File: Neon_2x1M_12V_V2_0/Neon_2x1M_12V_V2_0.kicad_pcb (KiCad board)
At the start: 2 copper layers, 60 x 59.5 mm, 32 parts, among them J2 Barrel_Jack_MountingPin, J6 Conn_01x03_Pin, J7 Screw_Terminal_01x02, J8 Screw_Terminal_01x02, Q1 IRLML2502TRPBF, Q2 IRLML2502TRPBF, SW1 SW_Push, SW2 SW_Push, U1 ESP32-WROOM-32, U3 LM2596T-ADJ

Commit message: updated production files
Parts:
- moved R7 2.67 mm to (166.0, 102.0)
- moved SW1 2.28 mm to (165.4, 107.5)
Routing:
- net ESP_EN: track 6.59 -> 11.3 mm
- net +3V3: track 75.4 -> 77.7 mm
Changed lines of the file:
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@@
 		(tags "connector JST NV vertical")
 		(property "Reference" "J8"
-			(at 9 4.55 0)
+			(at 8.7 4.15 0)
 			(layer "F.SilkS")
 			(effects
@@
 	(footprint "Resistor_SMD:R_1210_3225Metric_Pad1.30x2.65mm_HandSolder"
 		(layer "F.Cu")
-		(at 168.5 101 90)
+		(at 166.025 102 90)
 		(descr "Resistor SMD 1210 (3225 Metric), square (rectangular) end terminal, IPC-7351 nominal with elongated pad for handsoldering. (Body size source: IPC-SM-782 page 72, https://www.pcb-3d.com/wordpress/wp-content/uploads/ipc-sm-782a_amendment_1_and_2.pdf)")
 		(tags "resistor handsolder")
@@
 		(tags "LED handsolder")
 		(property "Reference" "D9"
-			(at -2 2 180)
+			(at 1.1 2.2 180)
 			(layer "F.SilkS")
 			(effects
@@
 		(tags "connector JST NV vertical")
 		(property "Reference" "J7"
-			(at 9 4.05 0)
+			(at 8.8 3.85 0)
 			(layer "F.SilkS")
 			(effects
@@
 	(footprint "TS_button_3_4_2:TS_button_3_4_2"
 		(layer "F.Cu")
-		(at 166.5 105.5)
+		(at 165.4 107.5)
 		(property "Reference" "SW1"
 			(at 0 2.5 0)
@@
 	)
 	(gr_text "RESET"
-		(at 163 110.5 0)
+		(at 161.9 112.8 0)
 		(layer "F.SilkS")
 		(effects
@@
 		)
 	)
+	(gr_text "+"
+		(at 209.9 125.9 0)
+		(layer "F.SilkS")
+		(effects
+			(font
+				(size 1.5 1.5)
+				(thickness 0.3)
+				(bold yes)
+			)
+			(justify left bottom)
+		)
+	)
+	(gr_text "+"
+		(at 210.3 110.8 0)
+		(layer "F.SilkS")
+		(effects
+			(font
+				(size 1.5 1.5)
+				(thickness 0.3)
+				(bold yes)
+			)
+			(justify left bottom)
+		)
+	)
 	(gr_text "+12V"
 		(at 212.5 141 0)
@@
 		)
 	)
+	(gr_text "-"
+		(at 211.6 121 90)
+		(layer "F.SilkS")
+		(effects
+			(font
+				(size 1.5 1.5)
+				(thickness 0.3)
+				(bold yes)
+			)
+			(justify left bottom)
+		)
+	)
+	(gr_text "-"
+		(at 211.8 106 90)
+		(layer "F.SilkS")
+		(effects
+			(font
+				(size 1.5 1.5)
+				(thickness 0.3)
+				(bold yes)
+			)
+			(justify left bottom)
+		)
+	)
 	(gr_text "+"
 		(at 206.5 126.5 0)
@@
 	)
 	(segment
-		(start 173.365 100.365)
-		(end 172 100.365)
+		(start 173.5 127.1)
+		(end 173.5 115.5)
 		(width 0.4)
 		(layer "F.Cu")
@@
 	)
 	(segment
+		(start 171.905 100.365)
+		(end 166.11 100.365)
+		(width 0.4)
+		(layer "F.Cu")
+		(net "+3V3")
+	)
+	(segment
 		(start 176.5 126)
 		(end 177.5 125)
@@
 	)
 	(segment
-		(start 173.5 127.1)
-		(end 173.5 115.5)
+		(start 166.11 100.365)
+		(end 166.025 100.45)
 		(width 0.4)
 		(layer "F.Cu")
@@
 	)
 	(segment
-		(start 172.1 128.5)
-		(end 173.5 127.1)
-		(width 0.4)
-		(layer "F.Cu")
-		(net "+3V3")
-	)
-	(segment
-		(start 171.905 100.365)
-		(end 169.635 100.365)
+		(start 173.365 100.365)
+		(end 172 100.365)
 		(width 0.4)
 		(layer "F.Cu")
@@
 	)
 	(segment
-		(start 175 102)
-		(end 173.365 100.365)
-		(width 0.4)
-		(layer "F.Cu")
-		(net "+3V3")
-	)
-	(segment
 		(start 188.45 127.35)
 		(end 188.3 127.5)
@@
 	)
 	(segment
-		(start 169.27 100)
-		(end 168.5 100)
-		(width 0.4)
-		(layer "F.Cu")
-		(net "+3V3")
-	)
-	(segment
 		(start 176.5 127)
 		(end 176.5 126)
@@
 	)
 	(segment
-		(start 169.635 100.365)
-		(end 169.27 100)
+		(start 172.1 128.5)
+		(end 173.5 127.1)
 		(width 0.4)
 		(layer "F.Cu")
@@
 	)
 	(segment
-		(start 191.45 132.4)
-		(end 191.45 127.6)
+		(start 175 102)
+		(end 173.365 100.365)
+		(width 0.4)
+		(layer "F.Cu")
+		(net "+3V3")
+	)
+	(segment
+		(start 191.55 132.3)
+		(end 191.55 127.5)
 		(width 0.4)
 		(layer "F.Cu")
@@
 	)
 	(segment
-		(start 191.55 127.5)
-		(end 194.45 127.5)
+		(start 191.45 132.4)
+		(end 191.55 132.3)
 		(width 0.4)
 		(layer "F.Cu")
@@
 	)
 	(segment
-		(start 191.45 127.6)
-		(end 191.55 127.5)
+		(start 191.55 127.5)
+		(end 194.45 127.5)
 		(width 0.4)
 		(layer "F.Cu")
@@
 	)
 	(segment
-		(start 196 114.05)
+		(start 200.44 114.05)
 		(end 198.5 114.05)
 		(width 0.4)
@@
 	)
 	(segment
-		(start 194.5 113.55)
-		(end 195.5 113.55)
+		(start 202.44 113.05)
+		(end 201.44 113.05)
 		(width 0.4)
 		(layer "F.Cu")
@@
 	)
 	(segment
-		(start 200.44 114.05)
-		(end 198.5 114.05)
+		(start 201.44 113.05)
+		(end 200.44 114.05)
 		(width 0.4)
 		(layer "F.Cu")
@@
 	)
 	(segment
-		(start 202.44 113.05)
-		(end 201.44 113.05)
+		(start 194.5 113.55)
+		(end 195.5 113.55)
 		(width 0.4)
 		(layer "F.Cu")
@@
 	)
 	(segment
-		(start 201.44 113.05)
-		(end 200.44 114.05)
+		(start 196 114.05)
+		(end 198.5 114.05)
 		(width 0.4)
 		(layer "F.Cu")
@@
 	)
 	(segment
-		(start 189.405 109.255)
-		(end 190.255 109.255)
+		(start 190.255 109.255)
+		(end 191.45 110.45)
 		(width 0.4)
 		(layer "F.Cu")
@@
 	)
 	(segment
-		(start 190.255 109.255)
-		(end 191.45 110.45)
+		(start 189.405 109.255)
+		(end 190.255 109.255)
 		(width 0.4)
 		(layer "F.Cu")
@@
 	)
 	(segment
-		(start 170 102)
-		(end 168.5 102)
+		(start 168.4 103.6)
+		(end 166.075 103.6)
 		(width 0.4)
 		(layer "F.Cu")
@@
 	)
 	(segment
-		(start 171.905 101.635)
-		(end 170.365 101.635)
+		(start 167.475 106.475)
+		(end 167.475 107.5)
 		(width 0.4)
 		(layer "F.Cu")
@@
 	)
 	(segment
-		(start 168.575 102.075)
-		(end 168.5 102)
+		(start 166.025 103.55)
+		(end 166.025 105.025)
+		(width 0.4)
+		(layer "F.Cu")
+		(net "ESP_EN")
+	)
+	(segment
+		(start 166.025 105.025)
+		(end 167.475 106.475)
 		(width 0.4)
 		(layer "F.Cu")
@@
 	(segment
 		(start 170.365 101.635)
-		(end 170 102)
+		(end 168.4 103.6)
 		(width 0.4)
 		(layer "F.Cu")
@@
 	)
 	(segment
-		(start 168.575 105)
-		(end 168.575 102.075)
+		(start 166.075 103.6)
+		(end 166.025 103.55)
+		(width 0.4)
+		(layer "F.Cu")
+		(net "ESP_EN")
+	)
+	(segment
+		(start 171.905 101.635)
+		(end 170.365 101.635)
 		(width 0.4)
 		(layer "F.Cu")
@@
 	)
 	(segment
+		(start 192.925 116.925)
+		(end 191.605 115.605)
+		(width 0.4)
+		(layer "F.Cu")
+		(net "ESP_IO0")
+	)
+	(segment
 		(start 191.605 115.605)
 		(end 189.405 115.605)
@@
 		(width 0.4)
 		(layer "F.Cu")
-		(net "ESP_IO0")
-	)
-	(segment
-		(start 192.925 116.925)
-		(end 191.605 115.605)
-		(width 0.4)
-		(layer "F.Cu")

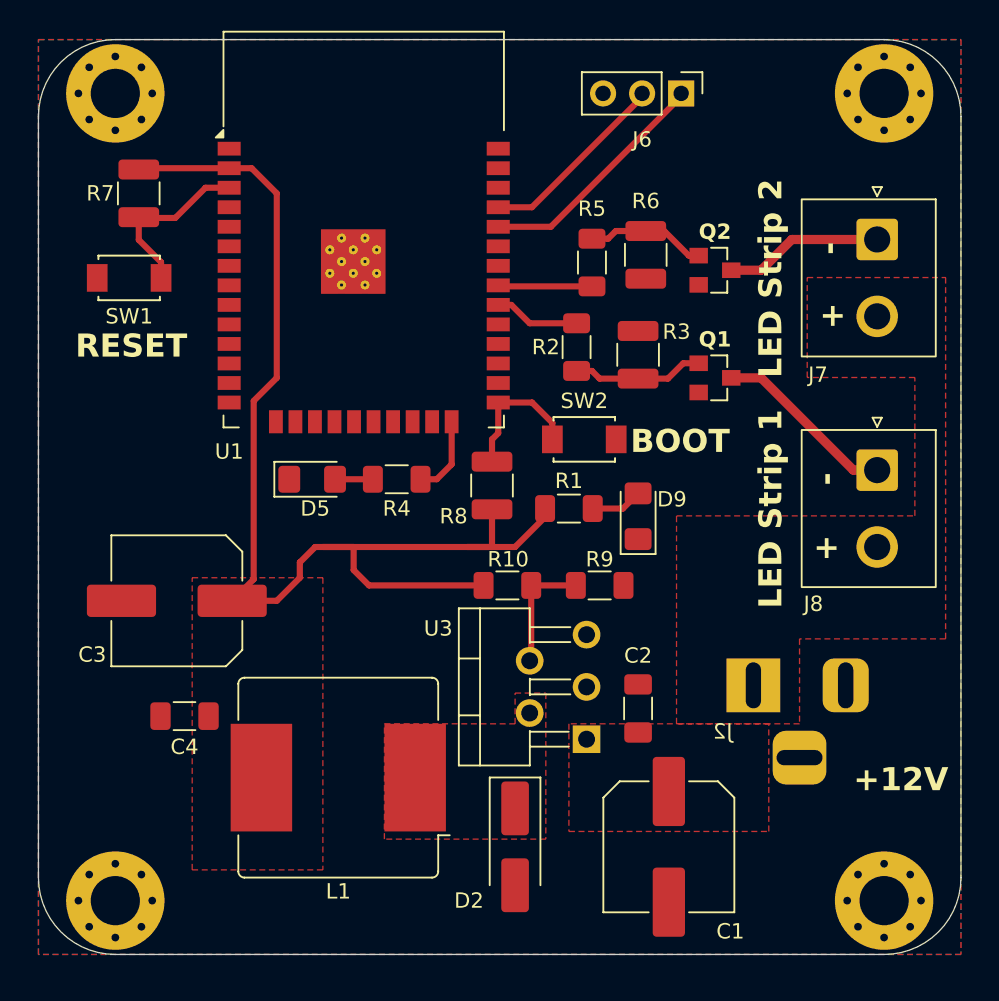
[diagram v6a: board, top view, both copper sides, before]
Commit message: updated layout and regenerated gerbers for manufacturer
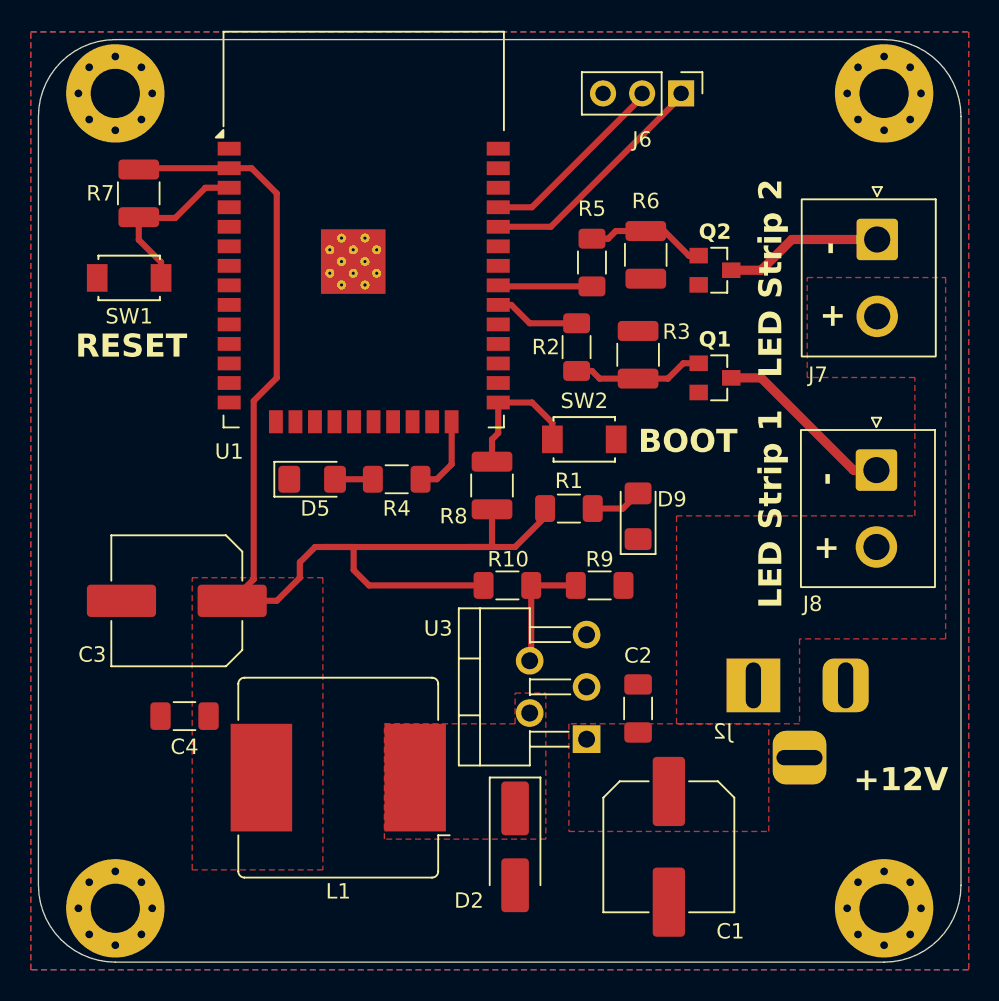
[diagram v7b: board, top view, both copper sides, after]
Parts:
- moved H1 0.50 mm to (164.5, 148.5)
- moved H3 0.50 mm to (214.5, 148.5)
- moved J8 0.05 mm to (214.0, 120.0)
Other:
- board size 60 x 59.5 mm -> 60 x 60 mm
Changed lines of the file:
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@@
 	(footprint "Connector_JST:JST_NV_B02P-NV_1x02_P5.00mm_Vertical"
 		(layer "F.Cu")
-		(at 214.05 120 -90)
+		(at 214 120 -90)
 		(descr "JST NV series connector, B02P-NV (http://www.jst-mfg.com/product/pdf/eng/eNV.pdf)")
 		(tags "connector JST NV vertical")
@@
 	(footprint "MountingHole:MountingHole_3.2mm_M3_Pad_Via"
 		(layer "F.Cu")
-		(at 214.5 148)
+		(at 214.5 148.5)
 		(descr "Mounting Hole 3.2mm, M3, generated by kicad-footprint-generator mountinghole.py")
 		(tags "mountinghole M3")
@@
 	(footprint "MountingHole:MountingHole_3.2mm_M3_Pad_Via"
 		(layer "F.Cu")
-		(at 164.5 148)
+		(at 164.5 148.5)
 		(descr "Mounting Hole 3.2mm, M3, generated by kicad-footprint-generator mountinghole.py")
 		(tags "mountinghole M3")
@@
 	)
 	(gr_line
-		(start 159.5 146.5)
+		(start 159.500048 146.999971)
 		(end 159.5 97)
 		(stroke
@@
 	)
 	(gr_arc
-		(start 164.5 151.5)
-		(mid 160.964466 150.035534)
-		(end 159.5 146.5)
+		(start 164.500048 151.999971)
+		(mid 160.964514 150.535505)
+		(end 159.500048 146.999971)
 		(stroke
 			(width 0.05)
@@
 	)
 	(gr_line
-		(start 214.5 151.5)
-		(end 164.5 151.5)
+		(start 214.5 152)
+		(end 164.5 152)
 		(stroke
 			(width 0.05)
@@
 	(gr_line
 		(start 219.5 97)
-		(end 219.5 146.5)
+		(end 219.500048 146.999963)
 		(stroke
 			(width 0.05)
@@
 	)
 	(gr_arc
-		(start 219.5 146.5)
-		(mid 218.035534 150.035534)
-		(end 214.5 151.5)
+		(start 219.500048 146.999963)
+		(mid 218.035582 150.535497)
+		(end 214.500048 151.999963)
 		(stroke
 			(width 0.05)
@@
 	)
 	(gr_text "BOOT"
-		(at 198 119 0)
+		(at 198.5 119 0)
 		(layer "F.SilkS")
 		(effects
@@
 		(layer "Cmts.User")
 		(pts
-			(xy 159.5 97) (xy 219.5 96.9)
+			(xy 214.5 92) (xy 214.5 151.999963)
 		)
-		(height -24.4)
-		(orientation 0)
+		(height 9)
+		(orientation 1)
 		(format
 			(prefix "")
@@
 		)
 		(gr_text "60"
-			(at 189.5 71.45 0)
+			(at 222.35 121.999982 90)
 			(layer "Cmts.User")
 			(effects
@@
 		(layer "Cmts.User")
 		(pts
-			(xy 214.5 92) (xy 214.5 151.5)
+			(xy 159.5 97) (xy 219.5 96.9)
 		)
-		(height 12)
-		(orientation 1)
+		(height -24.4)
+		(orientation 0)
 		(format
 			(prefix "")
@@
 			(keep_text_aligned yes)
 		)
-		(gr_text "59.5"
-			(at 225.35 121.75 90)
+		(gr_text "60"
+			(at 189.5 71.45 0)
 			(layer "Cmts.User")
 			(effects
@@
 	)
 	(segment
-		(start 214.05 120)
-		(end 212.5 120)
+		(start 212.5 120)
+		(end 206.5 114)
 		(width 0.6)
 		(layer "F.Cu")
@@
 	)
 	(segment
-		(start 212.5 120)
-		(end 206.5 114)
+		(start 214 120)
+		(end 212.5 120)
 		(width 0.6)
 		(layer "F.Cu")
@@
 		(polygon
 			(pts
-				(xy 159.5 92) (xy 219.5 92) (xy 219.5 151.5) (xy 159.5 151.5)
+				(xy 159 91.5) (xy 220 91.5) (xy 220 152.5) (xy 159 152.5)
 			)
 		)
